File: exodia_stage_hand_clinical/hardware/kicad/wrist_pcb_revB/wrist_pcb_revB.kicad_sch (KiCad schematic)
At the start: 25 parts, among them J1 USBC_16PIN, J2 ZIF_10PIN, Q1 AO3400A, U1 ESP32S3_MODULE, U2 TP4056_IC, U3 AP2112K, U4 DRV2605L_IC, U5 TS3A5017_IC

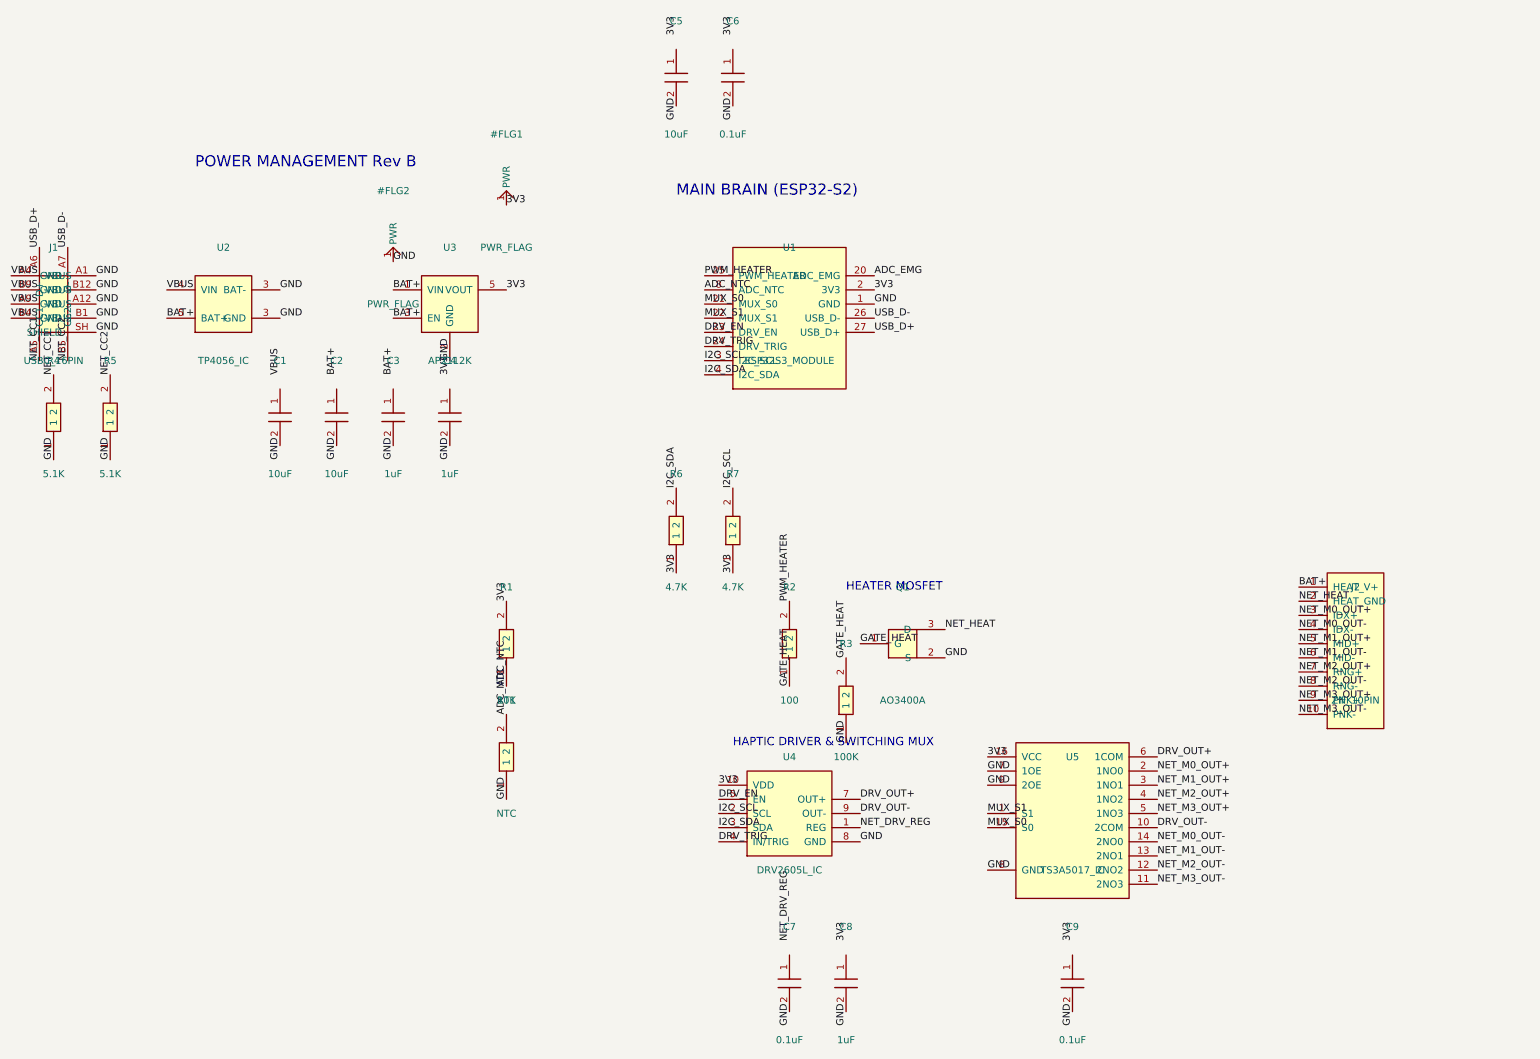
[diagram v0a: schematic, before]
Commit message: Implement Exodia Stage Hand Care Rev B: 20-pin ZIF, triple haptic trigger architecture, ground isolation, and care vocabulary
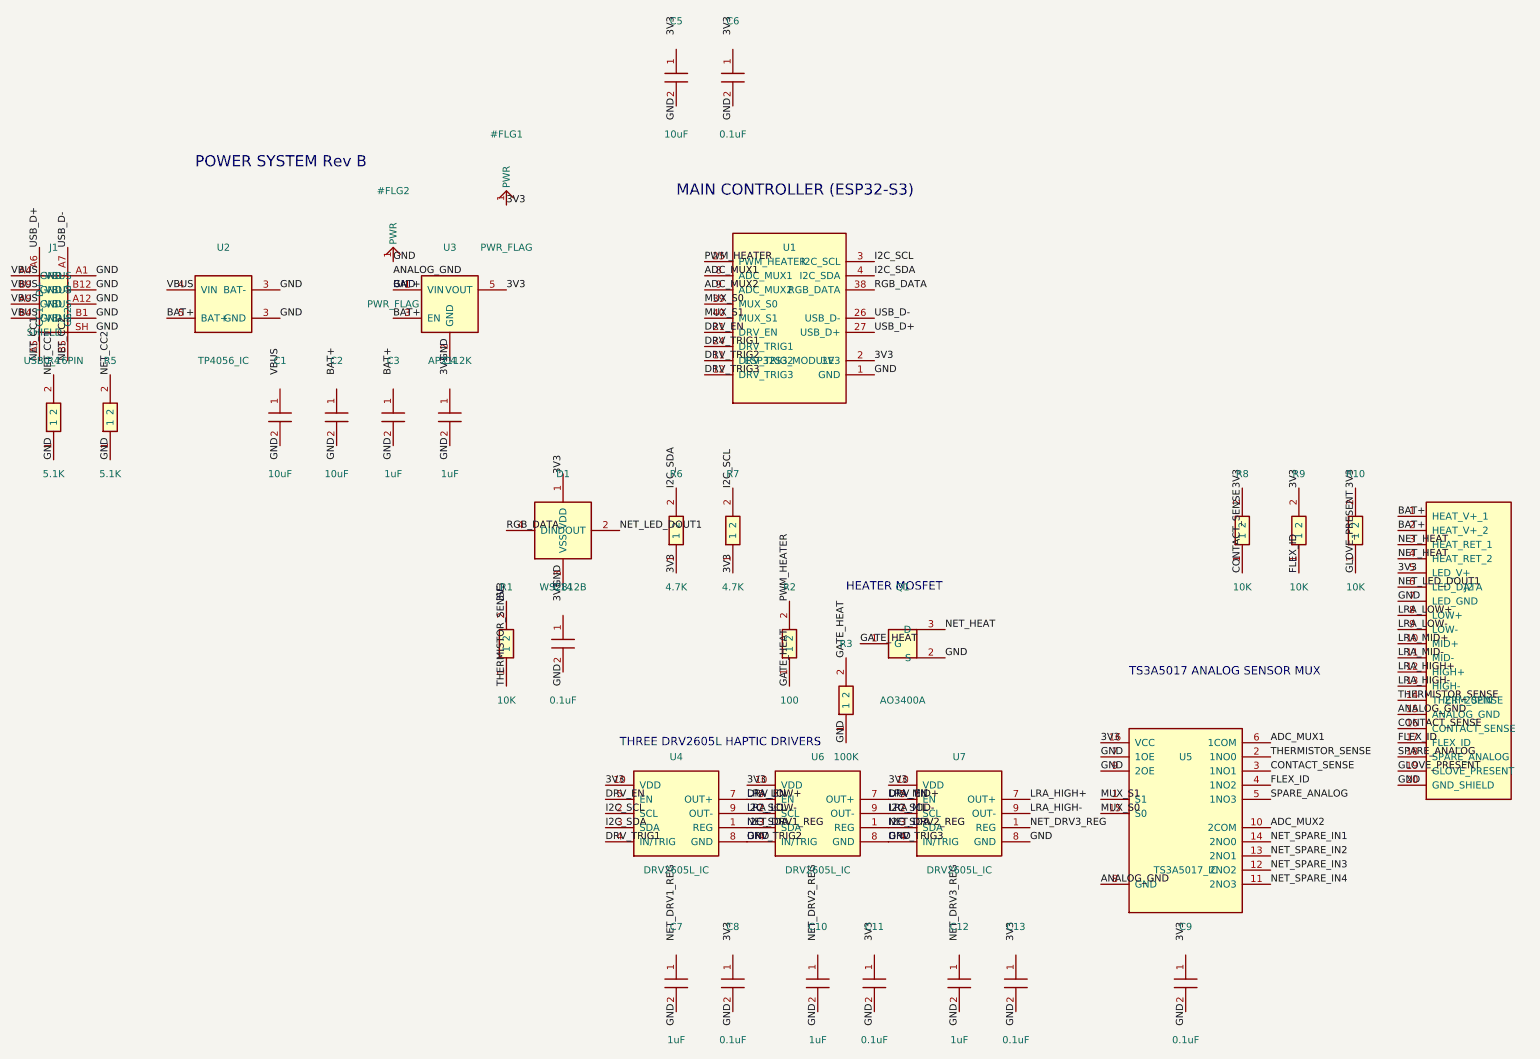
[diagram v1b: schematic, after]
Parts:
- removed J2: ZIF_10PIN, Connector_FFC-FPC:TE_1-1734839-0_1x10-1MP_P0.5mm_Horizontal, symbol ZIF_10PIN
- removed RT1: NTC, Resistor_SMD:R_0603_1608Metric, symbol NTC
- added C10, C12: 1uF, Capacitor_SMD:C_0603_1608Metric, symbol CAPACITOR
- added C11, C13, C14: 0.1uF, Capacitor_SMD:C_0603_1608Metric, symbol CAPACITOR
- added D1: WS2812B, LED_SMD:LED_WS2812B_PLCC4_5.0x5.0mm_P3.2mm, symbol WS2812B
- added J2: ZIF_20PIN, Connector_FFC-FPC:TE_1-1734839-0_1x20-1MP_P0.5mm_Horizontal, symbol ZIF_20PIN
- added R10, R8, R9: 10K, Resistor_SMD:R_0603_1608Metric, symbol RESISTOR
- added U6, U7: DRV2605L_IC, Package_SO:VSSOP-10_3.0x3.0mm_P0.5mm, symbol DRV2605L_IC
- C7: value 0.1uF -> 1uF
- C8: value 1uF -> 0.1uF
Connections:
- net NET_DRV_REG is gone; now on net I2C_SDA: U4.1 (REG)
- net 3V3: now also D1.1 (VDD), J2.5 (LED_V+), R10.2, R8.2, R9.2, U6.10 (VDD), U7.10 (VDD)
- net BAT+: now also J1.A1 (GND), J1.A12 (GND), J1.B1 (GND), J1.B12 (GND), J1.SH (SHIELD), Q1.2 (S), R3.1, R4.1, R5.1, U1.1 (GND), U1.11 (DRV_TRIG2), U1.12 (DRV_TRIG3), U2.3 (GND), U3.2 (GND), U4.8 (GND), U5.7 (1OE), U5.9 (2OE), D1.3 (VSS), J2.1 (HEAT_V+_1), J2.2 (HEAT_V+_2), J2.20 (GND_SHIELD), J2.7 (LED_GND), U6.4 (IN/TRIG), U6.8 (GND), U7.4 (IN/TRIG), U7.8 (GND)
- net DRV_EN: now also U1.21 (DRV_EN), U4.7 (OUT+), J2.10 (MID+), J2.8 (LOW+), U6.5 (EN), U6.7 (OUT+), U7.5 (EN); no longer U1.23 (DRV_EN)
- net I2C_SCL: now also U4.9 (OUT-), J2.11 (MID-), J2.9 (LOW-), U6.2 (SCL), U6.9 (OUT-), U7.2 (SCL)
- net I2C_SDA: now also U6.1 (REG), U6.3 (SDA), U7.3 (SDA)
- net MUX_S0: now also U1.39 (MUX_S0); no longer U1.21 (MUX_S0)
- net MUX_S1: now also U1.40 (MUX_S1); no longer U1.22 (MUX_S1)
- net NET_HEAT: now also J2.3 (HEAT_RET_1), J2.4 (HEAT_RET_2)
- removed net ADC_EMG: U1.20 (ADC_EMG)
- net ADC_NTC renamed ADC_MUX1
- net ADC_MUX1: now also U5.6 (1COM); no longer R1.1
- removed net DRV_OUT+: U4.7 (OUT+), U5.6 (1COM)
- net DRV_OUT- renamed ADC_MUX2
- net ADC_MUX2: now also U1.9 (ADC_MUX2); no longer U4.9 (OUT-)
- net DRV_TRIG renamed DRV_TRIG1
- removed net GND: J1.A1 (GND), J1.A12 (GND), J1.B1 (GND), J1.B12 (GND), J1.SH (SHIELD), Q1.2 (S), R3.1, R4.1, R5.1, U1.1 (GND), U2.3 (GND), U3.2 (GND), U4.8 (GND), U5.7 (1OE), U5.8 (GND), U5.9 (2OE)
- net NET_M0_OUT+ renamed THERMISTOR_SENSE
- net THERMISTOR_SENSE: now also R1.1, J2.14 (THERM_SENSE)
- net NET_M0_OUT- renamed NET_SPARE_IN1
- net NET_M1_OUT+ renamed CONTACT_SENSE
- net CONTACT_SENSE: now also J2.16 (CONTACT_SENSE), R8.1
- net NET_M1_OUT- renamed NET_SPARE_IN2
- net NET_M2_OUT+ renamed FLEX_ID
- net FLEX_ID: now also J2.17 (FLEX_ID), R9.1
- net NET_M2_OUT- renamed NET_SPARE_IN3
- net NET_M3_OUT+ renamed SPARE_ANALOG
- net SPARE_ANALOG: now also J2.18 (SPARE_ANALOG)
- net NET_M3_OUT- renamed NET_SPARE_IN4
- new net ANALOG_GND: J2.15 (ANALOG_GND), U5.8 (GND)
- new net GLOVE_PRESENT: J2.19 (GLOVE_PRESENT), R10.1
- new net LRA_HIGH+: J2.12 (HIGH+), U7.7 (OUT+)
- new net LRA_HIGH-: J2.13 (HIGH-), U7.9 (OUT-)
- new net NET_DRV3_REG: U7.1 (REG)
- new net NET_LED_DOUT1: D1.2 (DOUT), J2.6 (LED_DATA)
- new net RGB_DATA: D1.4 (DIN), U1.38 (RGB_DATA)
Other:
- note added: "MAIN CONTROLLER (ESP32-S3)"
- note added: "POWER SYSTEM Rev B"
- note added: "THREE DRV2605L HAPTIC DRIVERS"
- note added: "TS3A5017 ANALOG SENSOR MUX"
- note removed: "HAPTIC DRIVER & SWITCHING MUX"
- note removed: "MAIN BRAIN (ESP32-S2)"
- note removed: "POWER MANAGEMENT Rev B"
- title: Exodia Stage Hand - Clinical Wrist PCB (Rev B) -> Exodia Stage Hand - Care Edition Wrist PCB (Rev B)

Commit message: Resolve footprint loading errors by aligning MSOP-10 and TE FPC footprint prefixes with KiCad 10 standard libraries
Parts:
- J2: footprint Connector_FFC-FPC:TE_1-1734839-0_1x20-1MP_P0.5mm_Horizontal -> Connector_FFC-FPC:TE_2-1734839-0_1x20-1MP_P0.5mm_Horizontal
- U4, U6, U7: footprint Package_SO:VSSOP-10_3.0x3.0mm_P0.5mm -> Package_SO:MSOP-10_3x3mm_P0.5mm
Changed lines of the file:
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@@
     (property "Reference" "U4" (id 0) (at 132.08 157.48 0) (effects (font (size 1.27 1.27))))
     (property "Value" "DRV2605L_IC" (id 1) (at 132.08 177.79999999999998 0) (effects (font (size 1.27 1.27))))
-    (property "Footprint" "Package_SO:VSSOP-10_3.0x3.0mm_P0.5mm" (id 2) (at 132.08 167.64 0) (effects (hide yes)))
+    (property "Footprint" "Package_SO:MSOP-10_3x3mm_P0.5mm" (id 2) (at 132.08 167.64 0) (effects (hide yes)))
     (property "Datasheet" "" (id 3) (at 132.08 167.64 0) (effects (hide yes)))
   )
@@
     (property "Reference" "U6" (id 0) (at 157.48 157.48 0) (effects (font (size 1.27 1.27))))
     (property "Value" "DRV2605L_IC" (id 1) (at 157.48 177.79999999999998 0) (effects (font (size 1.27 1.27))))
-    (property "Footprint" "Package_SO:VSSOP-10_3.0x3.0mm_P0.5mm" (id 2) (at 157.48 167.64 0) (effects (hide yes)))
+    (property "Footprint" "Package_SO:MSOP-10_3x3mm_P0.5mm" (id 2) (at 157.48 167.64 0) (effects (hide yes)))
     (property "Datasheet" "" (id 3) (at 157.48 167.64 0) (effects (hide yes)))
   )
@@
     (property "Reference" "U7" (id 0) (at 182.88 157.48 0) (effects (font (size 1.27 1.27))))
     (property "Value" "DRV2605L_IC" (id 1) (at 182.88 177.79999999999998 0) (effects (font (size 1.27 1.27))))
-    (property "Footprint" "Package_SO:VSSOP-10_3.0x3.0mm_P0.5mm" (id 2) (at 182.88 167.64 0) (effects (hide yes)))
+    (property "Footprint" "Package_SO:MSOP-10_3x3mm_P0.5mm" (id 2) (at 182.88 167.64 0) (effects (hide yes)))
     (property "Datasheet" "" (id 3) (at 182.88 167.64 0) (effects (hide yes)))
   )
@@
     (property "Reference" "J2" (id 0) (at 274.32 127.0 0) (effects (font (size 1.27 1.27))))
     (property "Value" "ZIF_20PIN" (id 1) (at 274.32 147.32 0) (effects (font (size 1.27 1.27))))
-    (property "Footprint" "Connector_FFC-FPC:TE_1-1734839-0_1x20-1MP_P0.5mm_Horizontal" (id 2) (at 274.32 137.16 0) (effects (hide yes)))
+    (property "Footprint" "Connector_FFC-FPC:TE_2-1734839-0_1x20-1MP_P0.5mm_Horizontal" (id 2) (at 274.32 137.16 0) (effects (hide yes)))
     (property "Datasheet" "" (id 3) (at 274.32 137.16 0) (effects (hide yes)))
   )
